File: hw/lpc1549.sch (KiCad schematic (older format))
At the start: 16 parts, among them J301 ARM_JTAG_SWD_HEADER_10_PINSMD, U401 LPC1549JBD64, U402 MCP2551_SOIC8, X301 XTAL_7A-12.000MAAJ-T

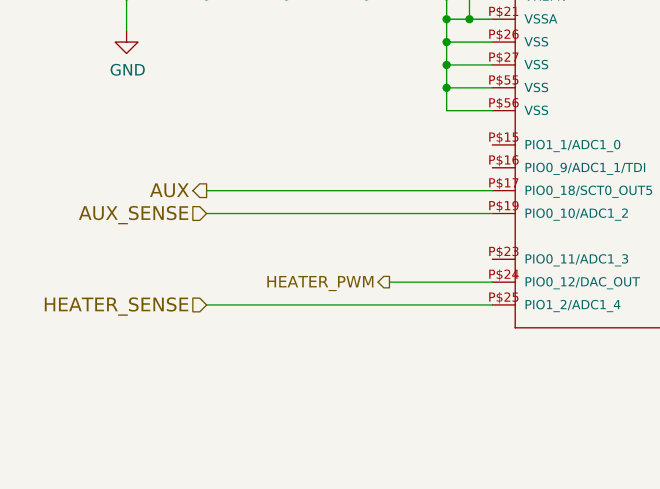
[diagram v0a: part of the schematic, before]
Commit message: hw 3.1.0 created. Fuel level moved from esb to fsb
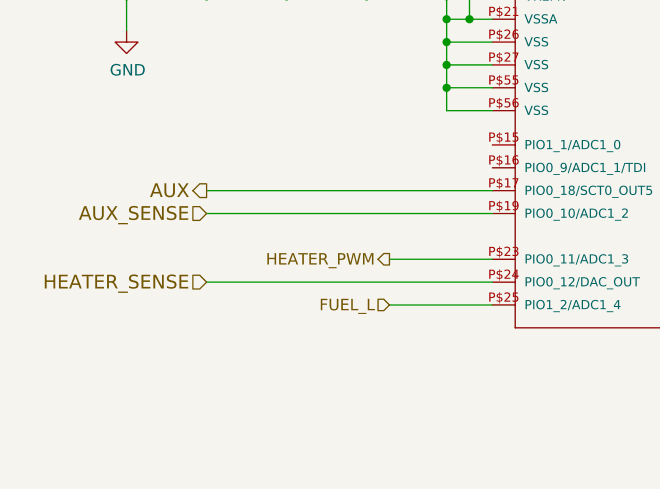
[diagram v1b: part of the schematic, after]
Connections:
- net HEATER_PWM: now also U401.P$23 (PIO0_11/ADC1_3); no longer U401.P$24 (PIO0_12/DAC_OUT)
- net HEATER_SENSE: now also U401.P$24 (PIO0_12/DAC_OUT); no longer U401.P$25 (PIO1_2/ADC1_4)
- new net FUEL_L: U401.P$25 (PIO1_2/ADC1_4)
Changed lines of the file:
@@
 Text HLabel 7150 2350 2    60   Input ~ 0
 EMCY
-Text HLabel 3350 5650 0    60   Input ~ 0
+Text HLabel 3350 5550 0    60   Input ~ 0
 HEATER_SENSE
 $Comp
@@
 	6400 2350 7150 2350
 Wire Wire Line
-	4600 5650 3350 5650
+	4600 5550 3350 5550
 Wire Wire Line
 	4600 2550 3350 2550
@@
 	10100 5700 10200 5700
 Wire Wire Line
-	4600 5550 4150 5550
-Text HLabel 4150 5550 0    50   Output ~ 0
+	4600 5450 4150 5450
+Text HLabel 4150 5450 0    50   Output ~ 0
 HEATER_PWM
+Wire Wire Line
+	4600 5650 4150 5650
+Text HLabel 4150 5650 0    50   Input ~ 0
+FUEL_L
 $EndSCHEMATC

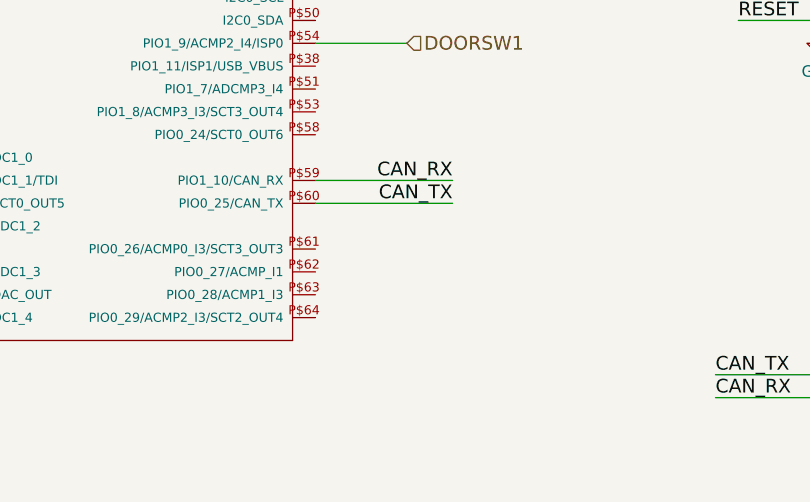
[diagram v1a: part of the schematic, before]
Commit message: 4.1.0 pcb ordered, with modified flyback diodes
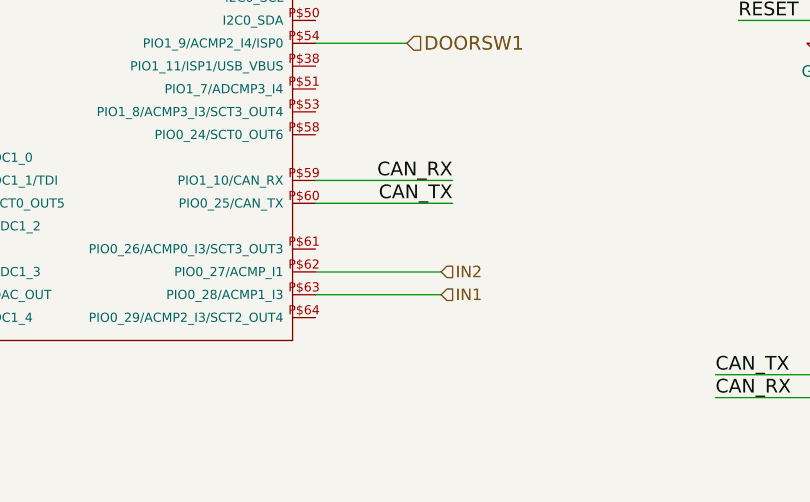
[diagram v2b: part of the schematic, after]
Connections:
- net IN2: now reaches U401.P$62 (PIO0_27/ACMP_I1)
- net IN1: now reaches U401.P$63 (PIO0_28/ACMP1_I3)
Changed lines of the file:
@@
 Text HLabel 4150 5650 0    50   Input ~ 0
 FUEL_L
+Wire Wire Line
+	6400 5550 6950 5550
+Wire Wire Line
+	6400 5450 6950 5450
+Text HLabel 6950 5550 2    50   Input ~ 0
+IN1
+Text HLabel 6950 5450 2    50   Input ~ 0
+IN2
 $EndSCHEMATC

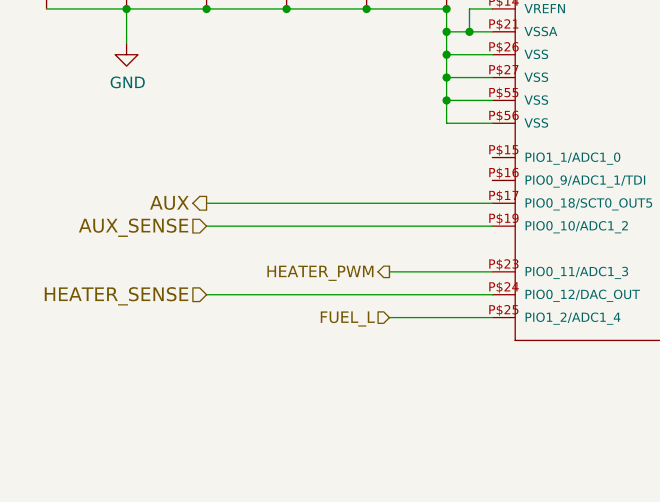
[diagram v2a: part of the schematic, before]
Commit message: pcb with heater push-pull control circuit
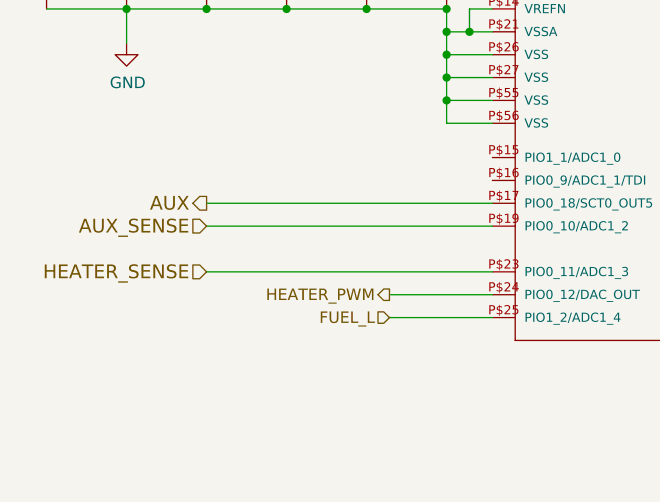
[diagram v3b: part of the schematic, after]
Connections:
- net HEATER_PWM: now also U401.P$24 (PIO0_12/DAC_OUT); no longer U401.P$23 (PIO0_11/ADC1_3)
- net HEATER_SENSE: now also U401.P$23 (PIO0_11/ADC1_3); no longer U401.P$24 (PIO0_12/DAC_OUT)
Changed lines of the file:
@@
 Text HLabel 7150 2350 2    60   Input ~ 0
 EMCY
-Text HLabel 3350 5550 0    60   Input ~ 0
+Text HLabel 3350 5450 0    60   Input ~ 0
 HEATER_SENSE
 $Comp
@@
 	6400 2350 7150 2350
 Wire Wire Line
-	4600 5550 3350 5550
+	4600 5450 3350 5450
 Wire Wire Line
 	4600 2550 3350 2550
@@
 	10100 5700 10200 5700
 Wire Wire Line
-	4600 5450 4150 5450
-Text HLabel 4150 5450 0    50   Output ~ 0
+	4600 5550 4150 5550
+Text HLabel 4150 5550 0    50   Output ~ 0
 HEATER_PWM
 Wire Wire Line

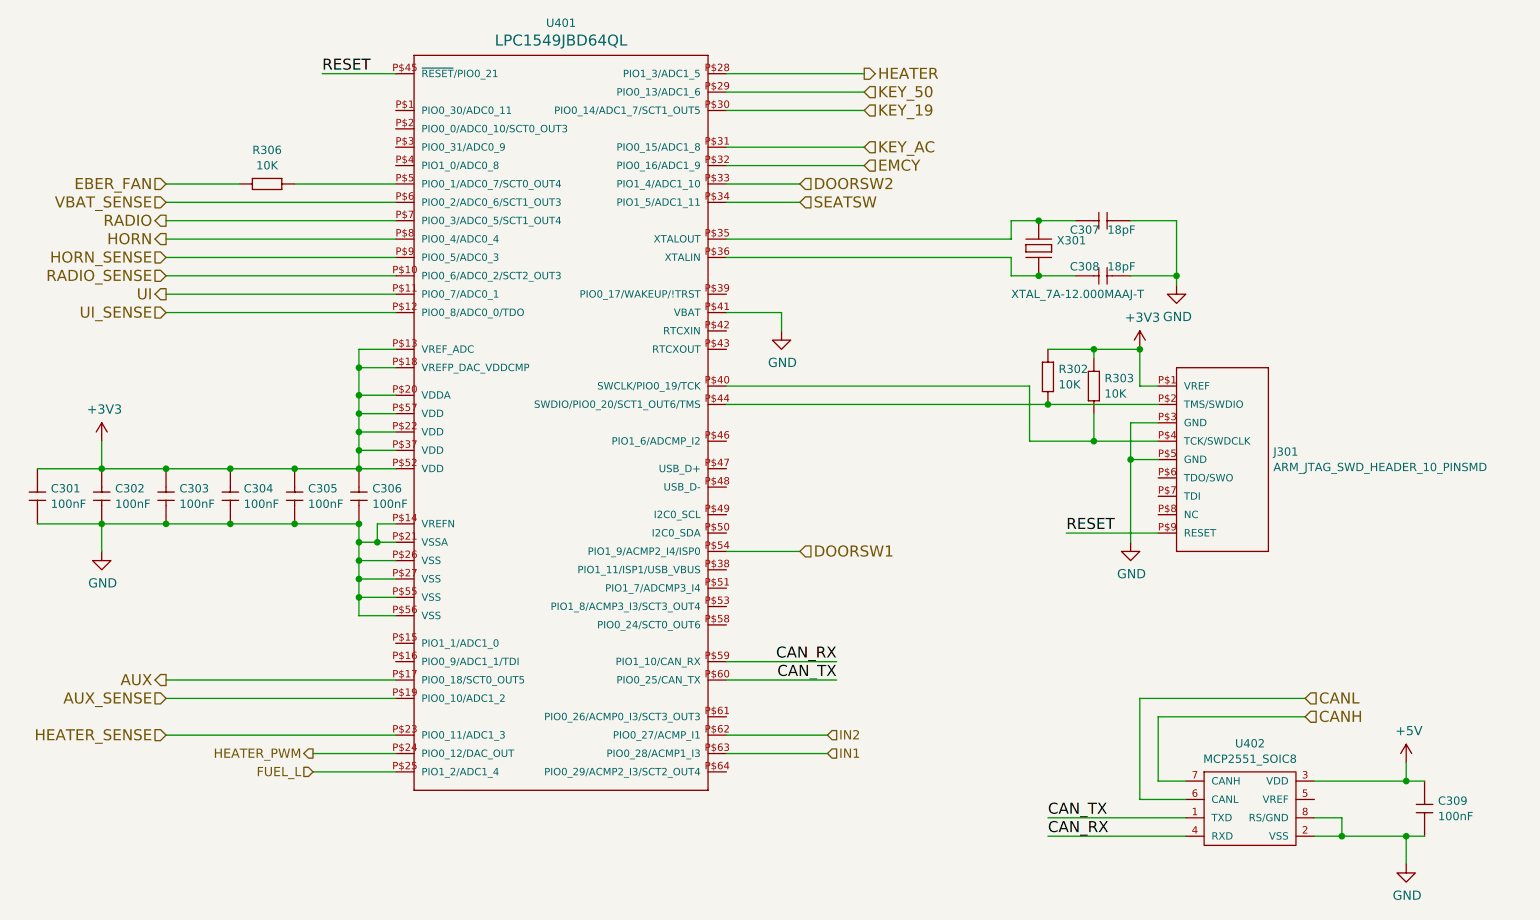
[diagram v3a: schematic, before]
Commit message: hw 6.0.0 created, fits uw aluminium enclosure
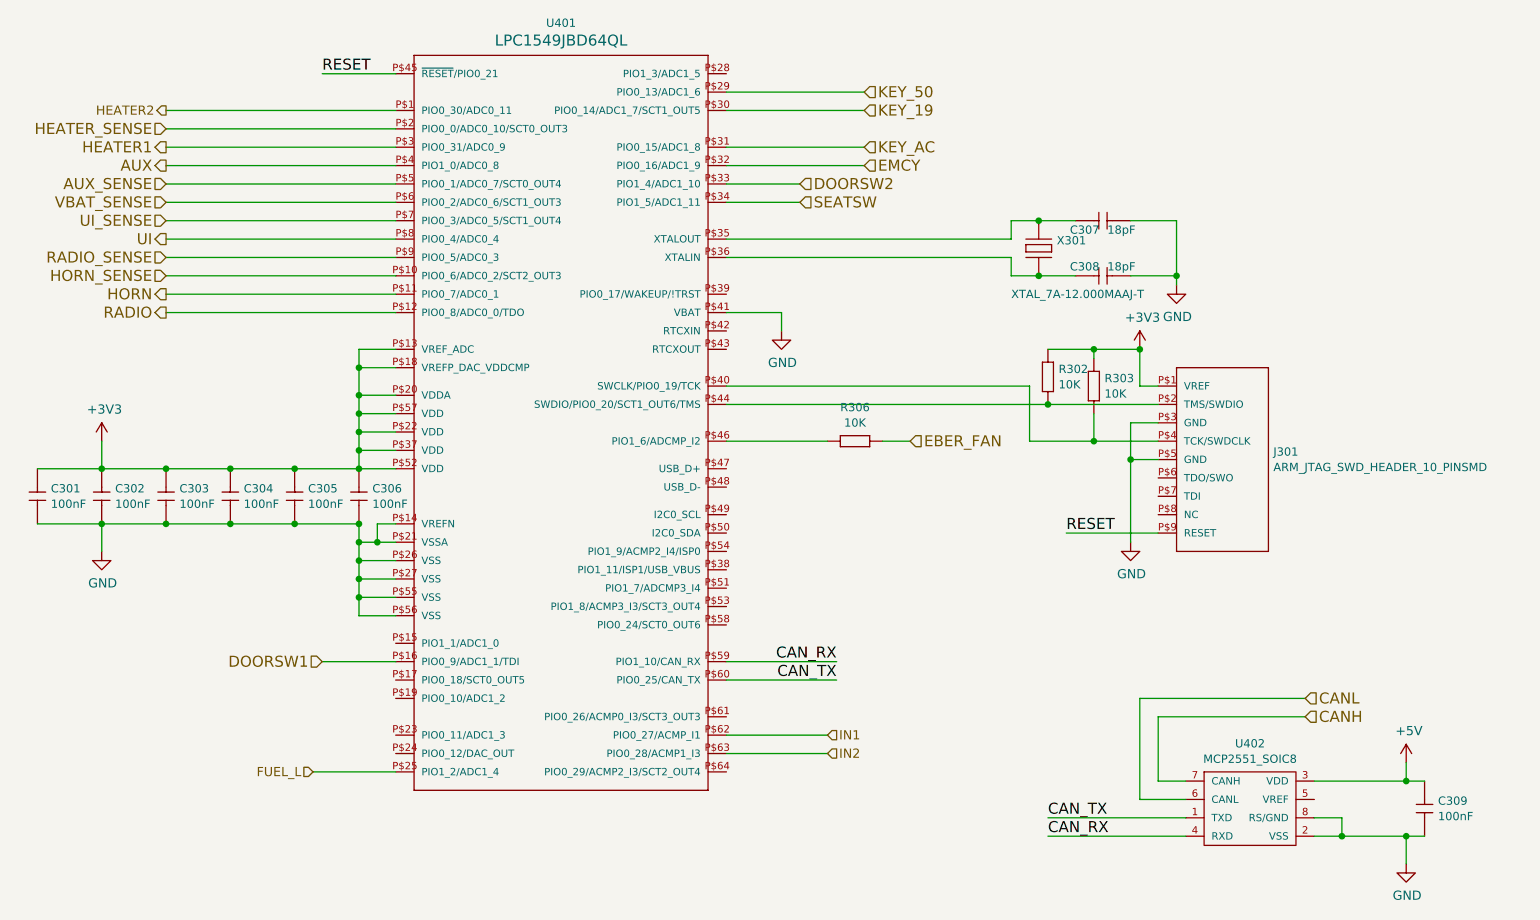
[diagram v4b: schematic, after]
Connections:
- net AUX: now also U401.P$4 (PIO1_0/ADC0_8); no longer U401.P$17 (PIO0_18/SCT0_OUT5)
- net AUX_SENSE: now also U401.P$5 (PIO0_1/ADC0_7/SCT0_OUT4); no longer U401.P$19 (PIO0_10/ADC1_2)
- net DOORSW1: now also U401.P$16 (PIO0_9/ADC1_1/TDI); no longer U401.P$54 (PIO1_9/ACMP2_I4/ISP0)
- net HEATER_SENSE: now also U401.P$2 (PIO0_0/ADC0_10/SCT0_OUT3); no longer U401.P$23 (PIO0_11/ADC1_3)
- net HORN: now also U401.P$11 (PIO0_7/ADC0_1); no longer U401.P$8 (PIO0_4/ADC0_4)
- net HORN_SENSE: now also U401.P$10 (PIO0_6/ADC0_2/SCT2_OUT3); no longer U401.P$9 (PIO0_5/ADC0_3)
- net IN1: now also U401.P$62 (PIO0_27/ACMP_I1); no longer U401.P$63 (PIO0_28/ACMP1_I3)
- net IN2: now also U401.P$63 (PIO0_28/ACMP1_I3); no longer U401.P$62 (PIO0_27/ACMP_I1)
- net RADIO: now also U401.P$12 (PIO0_8/ADC0_0/TDO); no longer U401.P$7 (PIO0_3/ADC0_5/SCT1_OUT4)
- net RADIO_SENSE: now also U401.P$9 (PIO0_5/ADC0_3); no longer U401.P$10 (PIO0_6/ADC0_2/SCT2_OUT3)
- net UI: now also U401.P$8 (PIO0_4/ADC0_4); no longer U401.P$11 (PIO0_7/ADC0_1)
- net UI_SENSE: now also U401.P$7 (PIO0_3/ADC0_5/SCT1_OUT4); no longer U401.P$12 (PIO0_8/ADC0_0/TDO)
- net at R306.1 (R1): now also U401.P$46 (PIO1_6/ADCMP_I2); no longer U401.P$5 (PIO0_1/ADC0_7/SCT0_OUT4)
- net HEATER2: now reaches U401.P$1 (PIO0_30/ADC0_11)
- net HEATER1: now reaches U401.P$3 (PIO0_31/ADC0_9)
- net HEATER: no longer names the net of U401.P$28 (PIO1_3/ADC1_5)
- net HEATER_PWM: no longer names the net of U401.P$24 (PIO0_12/DAC_OUT)
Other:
- moved on the sheet: R306
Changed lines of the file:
@@
 $Descr A4 11693 8268
 encoding utf-8
-Sheet 4 8
+Sheet 3 8
 Title ""
 Date ""
@@
 	1    0    0    -1
 $EndComp
+Text HLabel 7400 3850 2    60   Input ~ 0
+EBER_FAN
+Text HLabel 3350 3050 0    60   Output ~ 0
+HORN
+Text HLabel 3350 2950 0    60   Input ~ 0
+HORN_SENSE
+Text HLabel 3350 3150 0    60   Output ~ 0
+RADIO
+Text HLabel 3350 2850 0    60   Input ~ 0
+RADIO_SENSE
 Text HLabel 3350 2450 0    60   Input ~ 0
-EBER_FAN
-Text HLabel 3350 2750 0    60   Output ~ 0
-HORN
-Text HLabel 3350 2850 0    60   Input ~ 0
-HORN_SENSE
-Text HLabel 3350 2650 0    60   Output ~ 0
-RADIO
-Text HLabel 3350 2950 0    60   Input ~ 0
-RADIO_SENSE
-Text HLabel 3350 5250 0    60   Input ~ 0
 AUX_SENSE
-Text HLabel 3350 5150 0    60   Output ~ 0
+Text HLabel 3350 2350 0    60   Output ~ 0
 AUX
-Text HLabel 7150 1850 2    60   Output ~ 0
-HEATER
+Text HLabel 3350 2250 0    60   Output ~ 0
+HEATER1
 Text HLabel 7150 2050 2    60   Input ~ 0
 KEY_19
@@
 Text HLabel 7150 2350 2    60   Input ~ 0
 EMCY
-Text HLabel 3350 5450 0    60   Input ~ 0
+Text HLabel 3350 2150 0    60   Input ~ 0
 HEATER_SENSE
 $Comp
 L fsb-rescue:10K R306
 U 1 1 598BBA44
-P 3850 2450
-F 0 "R306" H 3900 2634 45  0000 C CNN
-F 1 "10K" H 3900 2550 45  0000 C CNN
-F 2 "multicomp:0603" H 3880 2600 20  0001 C CNN
-F 3 "http://www.farnell.com/datasheets/1788326.pdf?_ga=1.214208087.1948984246.1460023966" H 3819 2489 60  0001 C CNN
-F 4 "9330399" H 4219 2889 60  0001 C CNN "1st Source Part Number"
-F 5 "Farnell" H 4119 2789 60  0001 C CNN "1st Source"
-F 6 "MC0063W0603110K" H 4019 2689 60  0001 C CNN "Manufacturer Part Number"
-F 7 "MULTICOMP" H 3919 2589 60  0001 C CNN "Manufacturer"
-	1    3850 2450
-	1    0    0    -1
+P 7150 3850
+F 0 "R306" H 7200 4034 45  0000 C CNN
+F 1 "10K" H 7200 3950 45  0000 C CNN
+F 2 "multicomp:0603" H 7180 4000 20  0001 C CNN
+F 3 "http://www.farnell.com/datasheets/1788326.pdf?_ga=1.214208087.1948984246.1460023966" H 7119 3889 60  0001 C CNN
+F 4 "9330399" H 7519 4289 60  0001 C CNN "1st Source Part Number"
+F 5 "Farnell" H 7419 4189 60  0001 C CNN "1st Source"
+F 6 "MC0063W0603110K" H 7319 4089 60  0001 C CNN "Manufacturer Part Number"
+F 7 "MULTICOMP" H 7219 3989 60  0001 C CNN "Manufacturer"
+	1    7150 3850
+	-1   0    0    -1
 $EndComp
 Text HLabel 3350 2550 0    60   Input ~ 0
@@
 Connection ~ 10100 5700
 Wire Wire Line
-	4050 2450 4600 2450
-Wire Wire Line
-	3750 2450 3350 2450
-Wire Wire Line
-	4600 2750 3350 2750
+	6950 3850 6400 3850
+Wire Wire Line
+	7250 3850 7400 3850
+Wire Wire Line
+	4600 3050 3350 3050
+Wire Wire Line
+	4600 2950 3350 2950
+Wire Wire Line
+	4600 3150 3350 3150
 Wire Wire Line
 	4600 2850 3350 2850
 Wire Wire Line
-	4600 2650 3350 2650
-Wire Wire Line
-	4600 2950 3350 2950
-Wire Wire Line
-	4600 5250 3350 5250
-Wire Wire Line
-	4600 5150 3350 5150
-Wire Wire Line
-	6400 1850 7150 1850
+	4600 2450 3350 2450
+Wire Wire Line
+	4600 2350 3350 2350
+Wire Wire Line
+	4600 2250 3350 2250
 Wire Wire Line
 	6400 2250 7150 2250
@@
 	6400 2350 7150 2350
 Wire Wire Line
-	4600 5450 3350 5450
+	4600 2150 3350 2150
 Wire Wire Line
 	4600 2550 3350 2550
@@
 $EndComp
 Wire Wire Line
-	4600 3050 3350 3050
-Wire Wire Line
-	4600 3150 3350 3150
-Text HLabel 3350 3050 0    60   Output ~ 0
+	4600 2750 3350 2750
+Wire Wire Line
+	4600 2650 3350 2650
+Text HLabel 3350 2750 0    60   Output ~ 0
 UI
-Text HLabel 3350 3150 0    60   Input ~ 0
+Text HLabel 3350 2650 0    60   Input ~ 0
 UI_SENSE
 Wire Wire Line
@@
 Wire Wire Line
 	6400 2550 6800 2550
-Text HLabel 6800 4450 2    60   Input ~ 0
+Text HLabel 4200 5050 0    60   Input ~ 0
 DOORSW1
 Text HLabel 6800 2450 2    60   Input ~ 0
 DOORSW2
 Wire Wire Line
-	6400 4450 6800 4450
+	4600 5050 4200 5050
 Text HLabel 6800 2550 2    60   Input ~ 0
 SEATSW
@@
 	10100 5700 10200 5700
 Wire Wire Line
-	4600 5550 4150 5550
-Text HLabel 4150 5550 0    50   Output ~ 0
-HEATER_PWM
+	4600 2050 3350 2050
+Text HLabel 3350 2050 0    50   Output ~ 0
+HEATER2
 Wire Wire Line
 	4600 5650 4150 5650
@@
 FUEL_L
 Wire Wire Line
+	6400 5450 6950 5450
+Wire Wire Line
 	6400 5550 6950 5550
-Wire Wire Line
-	6400 5450 6950 5450
+Text HLabel 6950 5450 2    50   Input ~ 0
+IN1
 Text HLabel 6950 5550 2    50   Input ~ 0
-IN1
-Text HLabel 6950 5450 2    50   Input ~ 0
 IN2
 $EndSCHEMATC

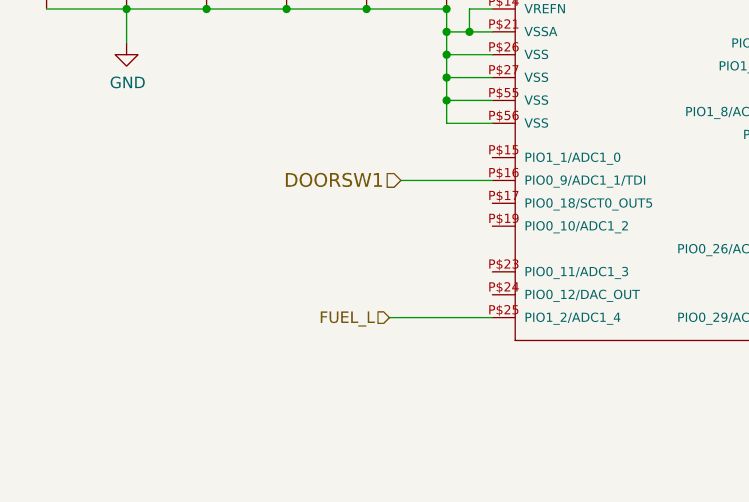
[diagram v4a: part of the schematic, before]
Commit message: coolvalve added to fsb
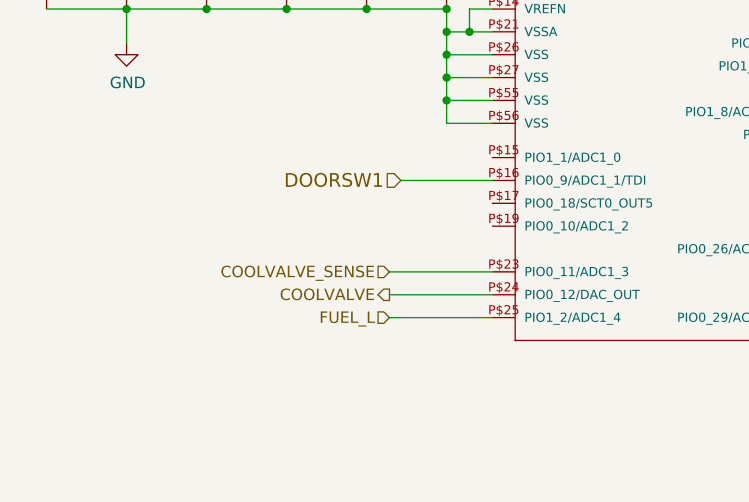
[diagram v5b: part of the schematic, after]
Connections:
- net COOLVALVE_SENSE: now reaches U401.P$23 (PIO0_11/ADC1_3)
- net COOLVALVE: now reaches U401.P$24 (PIO0_12/DAC_OUT)
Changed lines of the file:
@@
 $Descr A4 11693 8268
 encoding utf-8
-Sheet 3 8
+Sheet 3 9
 Title ""
 Date ""
@@
 Text HLabel 6950 5550 2    50   Input ~ 0
 IN2
+Wire Wire Line
+	4600 5550 4150 5550
+Wire Wire Line
+	4600 5450 4150 5450
+Text HLabel 4150 5550 0    50   Output ~ 0
+COOLVALVE
+Text HLabel 4150 5450 0    50   Input ~ 0
+COOLVALVE_SENSE
 $EndSCHEMATC
